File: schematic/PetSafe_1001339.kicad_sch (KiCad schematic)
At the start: 150 parts, among them J1 ICSP, J3 PIR BOARD, J5 MOTOR, J6 DNP, Q1 FMOS3401A?, Q11 MMBTA55?, Q2 BC847B?, Q3 MMBTA55?, Q4 MMBTA55?, Q5 MMBTA55?, Q6 MMBTA55?, Q7 BC857C?, Q8 SIL3724A?, Q9 DNP, U1 S-1200B45?, U106 U6A / DNP, U2 SN74LVC2G14DBV?, U3 SGM8542XS, U4 PIC16F18855, U5 MX512H, U6 S-812C33AMC? / 3.3V, U7 DNP, Y1 20 MHz

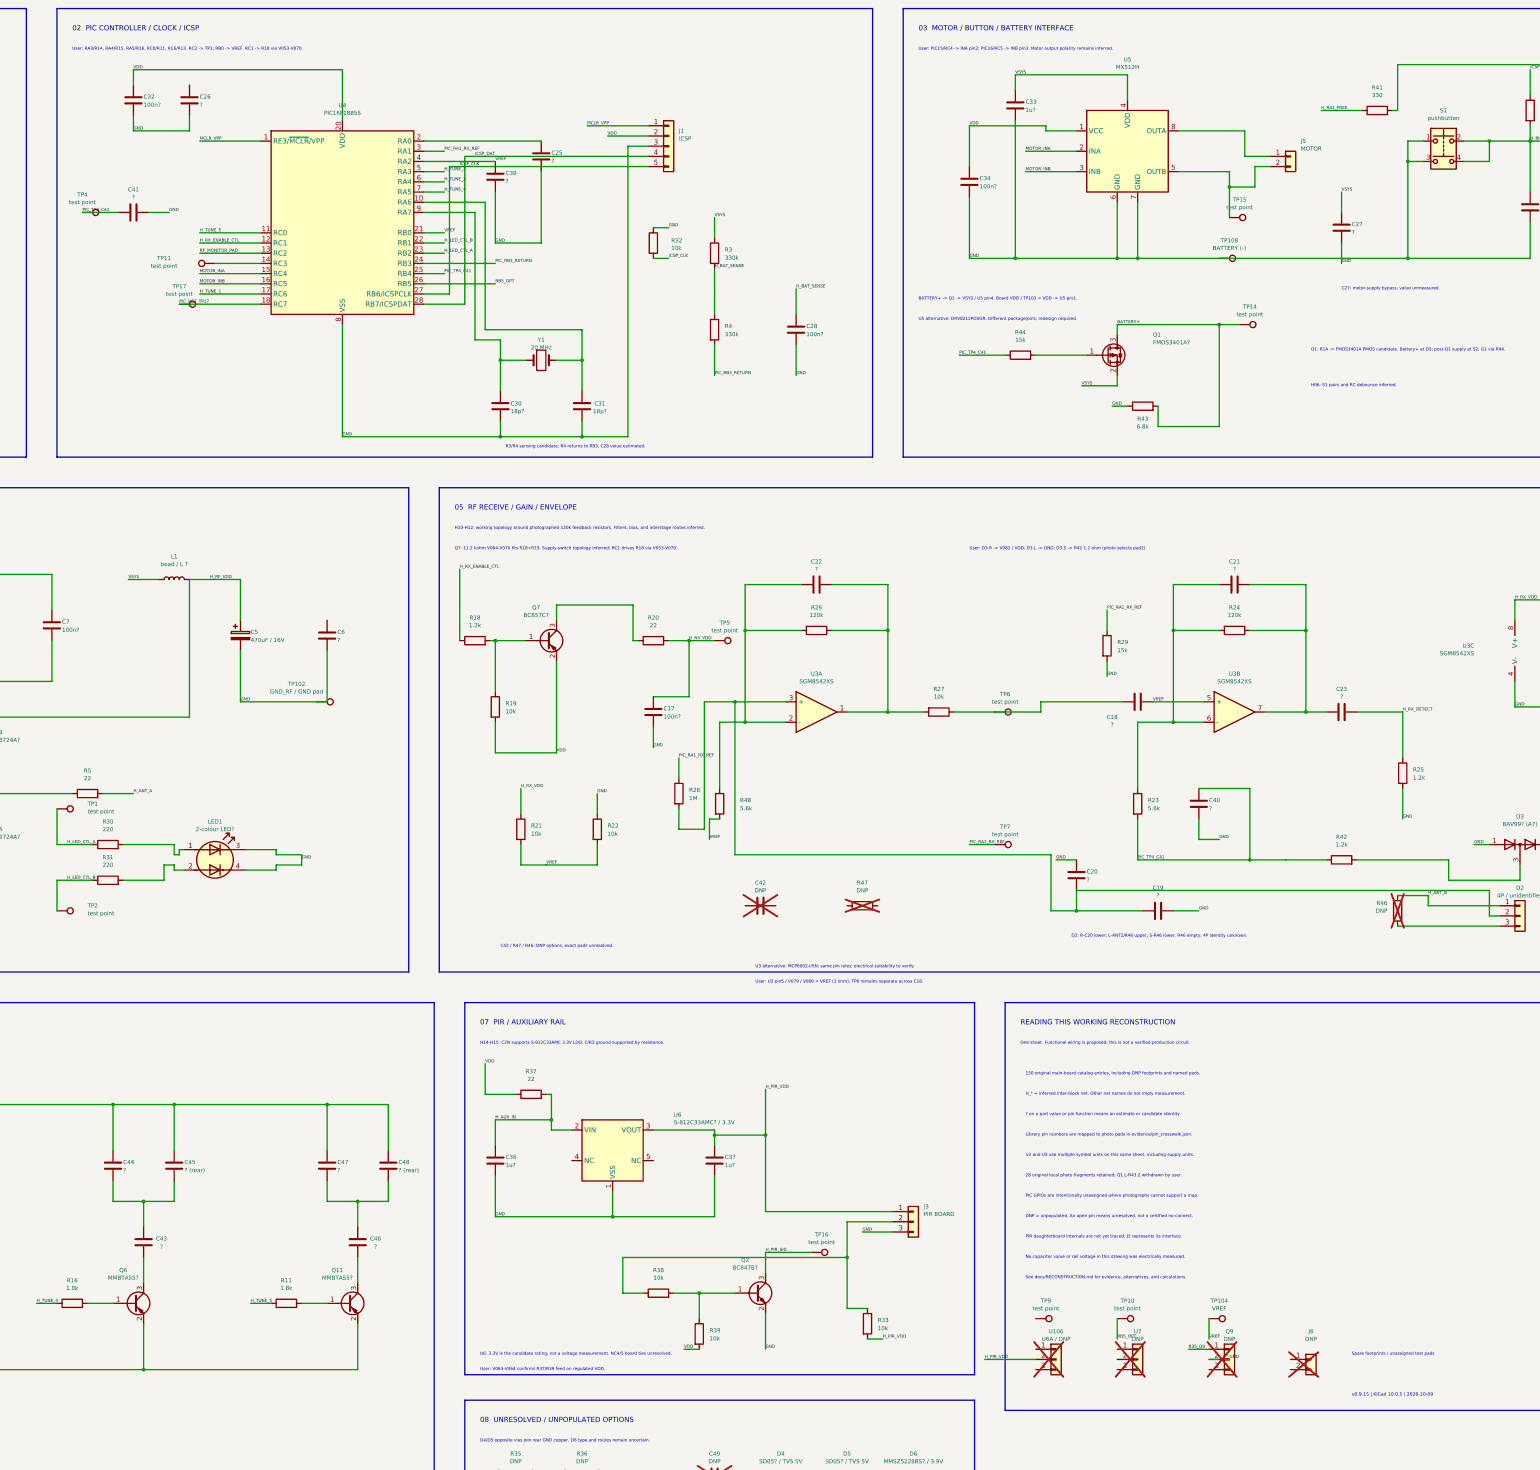
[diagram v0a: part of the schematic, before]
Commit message: Map U7 PIR connector and correct RB0 signal route
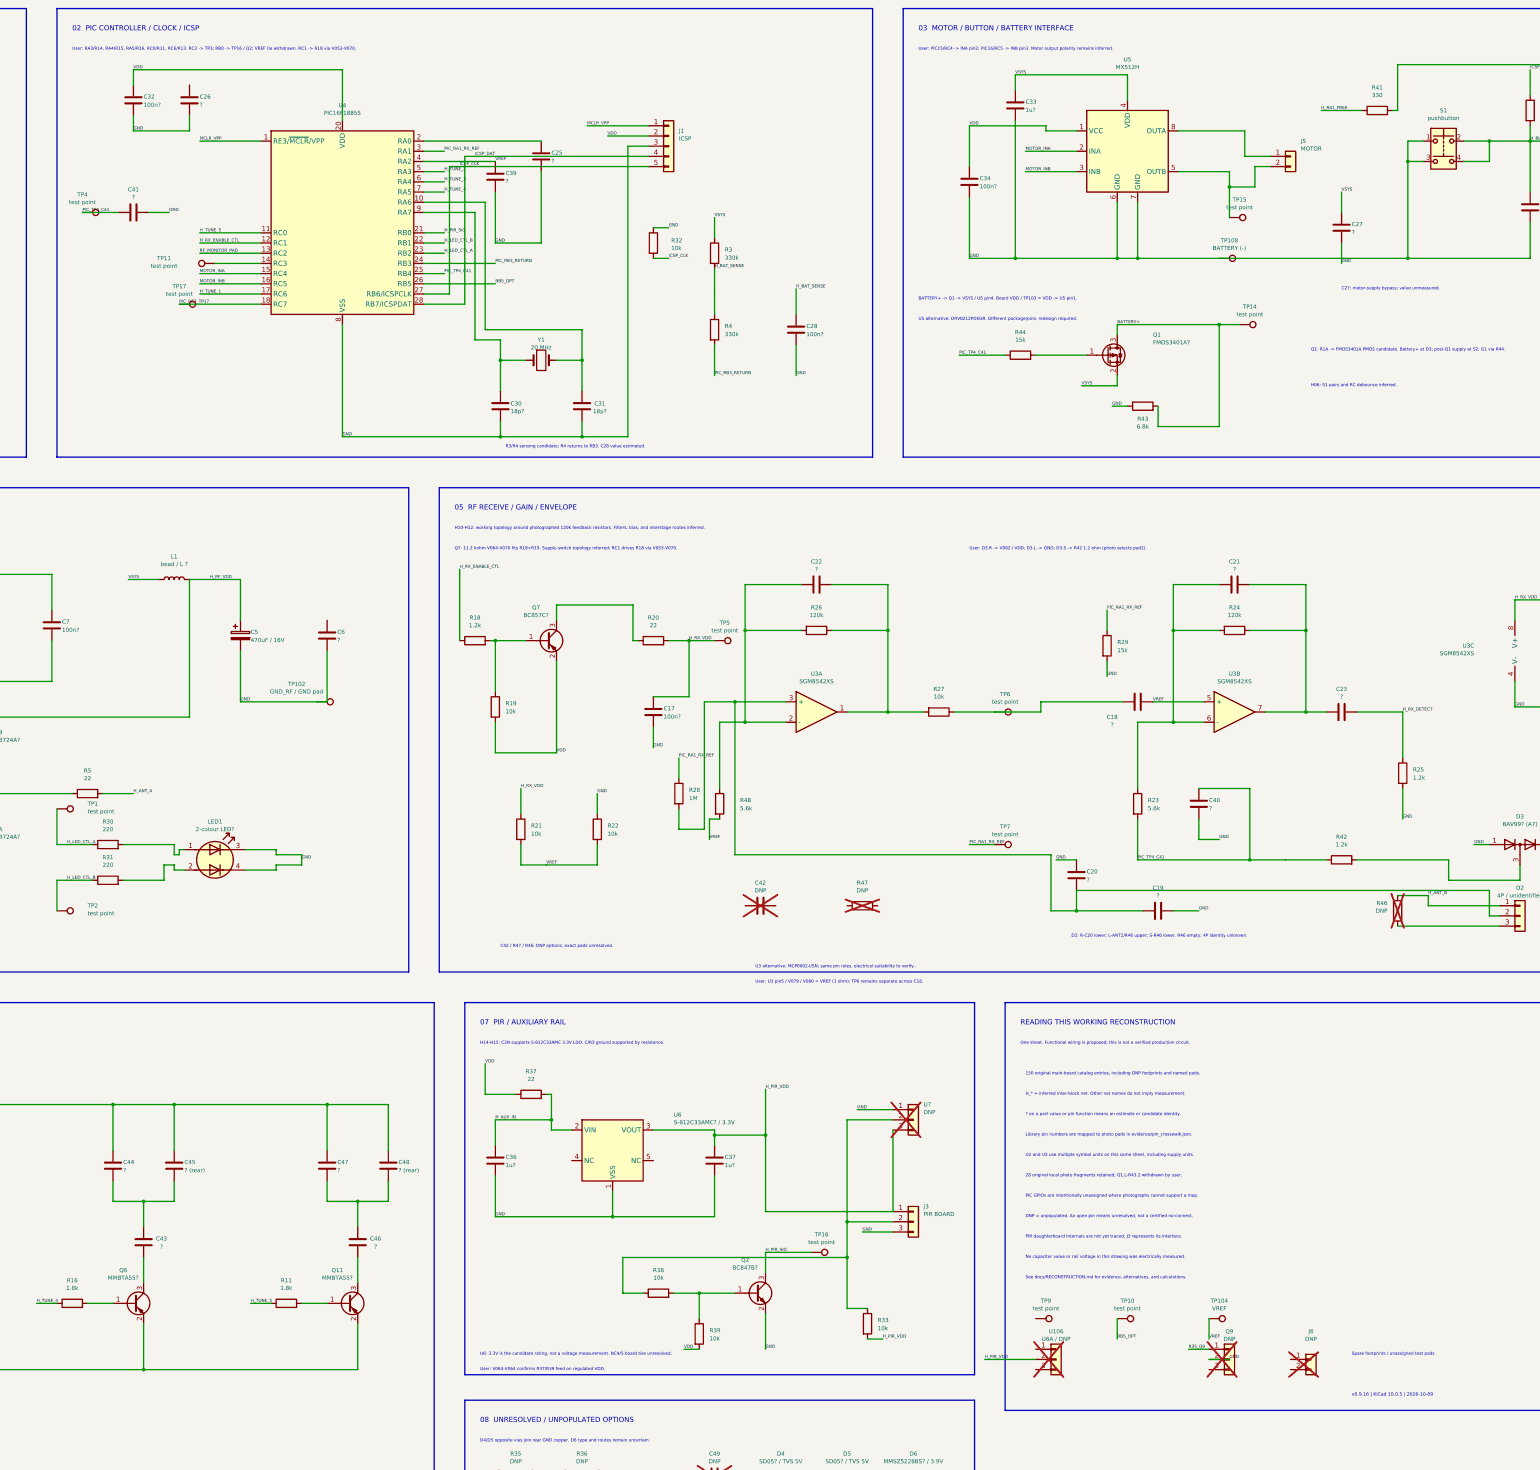
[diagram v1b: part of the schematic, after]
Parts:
- J3: MeasurementEvidence v0.9.14 user: pin1 PIR supply previously confirmed; pin2 H-R38 K/right/model1 1 ohm and H-R38 J/left/model2 10 kohm; pin3-GND 1 ohm. Pin2-GND remains 290 kohm (batch1), distinct from ground. Q2 onward/controller route remains unverified. -> v0.9.14 user: pin1 PIR supply previously confirmed; pin2 H-R38 K/right/model1 1 ohm and H-R38 J/left/model2 10 kohm; pin3-GND 1 ohm. Pin2-GND remains 290 kohm (batch1), distinct from ground. Q2 onward/controller route remains unverified. v0.9.16: matching physical columns reach U7; J3.1-U7.3 supply, J3.2-U7.2 signal, J3.3-U7.1 GND.; ViaEvidence v0.9.14 user: pin1 PIR supply previously confirmed; pin2 H-R38 K/right/model1 1 ohm and H-R38 J/left/model2 10 kohm; pin3-GND 1 ohm. Pin2-GND remains 290 kohm (batch1), distinct from ground. Q2 onward/controller route remains unverified. -> v0.9.14 user: pin1 PIR supply previously confirmed; pin2 H-R38 K/right/model1 1 ohm and H-R38 J/left/model2 10 kohm; pin3-GND 1 ohm. Pin2-GND remains 290 kohm (batch1), distinct from ground. Q2 onward/controller route remains unverified. v0.9.16: matching physical columns reach U7; J3.1-U7.3 supply, J3.2-U7.2 signal, J3.3-U7.1 GND.
- R21, R48: MeasurementEvidence (none) -> v0.9.16 CORRECTION: user confirms PIC21/RB0 -> TP16 -> Q2 s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; ViaEvidence v0.9.8: User confirms V071-VREF. Earlier V071-R21.2 and V02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 -> v0.9.16 CORRECTION: user confirms PIC21/RB0 -> TP16 -> Q2 s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
- R22: MeasurementEvidence v0.9.14 user: E/right/model1-GND 1 ohm; D/left/model2-VREF 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 -> v0.9.16 CORRECTION: user confirms PIC21/RB0 -> TP16 -> Q2 s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; ViaEvidence v0.9.14 user: E/right/model1-GND 1 ohm; D/left/model2-VREF 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 -> v0.9.16 CORRECTION: user confirms PIC21/RB0 -> TP16 -> Q2 s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
- TP104, U4: MeasurementEvidence (none) -> v0.9.16 CORRECTION: user confirms PIC21/RB0 -> TP16 -> Q2 s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; ViaEvidence v0.9.9: User checked V035-VREF TP. Prior photo association 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 -> v0.9.16 CORRECTION: user confirms PIC21/RB0 -> TP16 -> Q2 s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
- TP16: MeasurementEvidence (none) -> v0.9.16 CORRECTION: user confirms PIC21/RB0 -> TP16 -> Q2 s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; ViaEvidence (none) -> v0.9.16 CORRECTION: user confirms PIC21/RB0 -> TP16 -> Q2 s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
- U7: MeasurementEvidence (none) -> v0.9.16: user measured U7 square pad/model1 to J3.3/GND; mi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; ViaEvidence (none) -> v0.9.16: user measured U7 square pad/model1 to J3.3/GND; mi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
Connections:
- net GND: now also U7.1 (Pin_1)
- net H_PIR_SIG: now also U4.21 (RB0)
- net H_PIR_VDD: now also U7.3 (Pin_3)
- net VREF: no longer U4.21 (RB0)
- net at J3.2 (Pin_2), R33.1, R38.1: now also U7.2 (Pin_2)
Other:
- note added: "User: RA3/R14, RA4/R15, RA5/R16, RC0/R11, RC6/R13. RC2 -> TP3; RB0 -> TP16 / Q2; VREF tie withdrawn. RC1 -> R18 via V053-V070."
- note added: "v0.9.16 | KiCad 10.0.5 | 2026-10-09"
- note removed: "User: RA3/R14, RA4/R15, RA5/R16, RC0/R11, RC6/R13. RC2 -> TP3; RB0 -> VREF. RC1 -> R18 via V053-V070."
- note removed: "v0.9.15 | KiCad 10.0.5 | 2026-10-09"
- moved on the sheet: U7

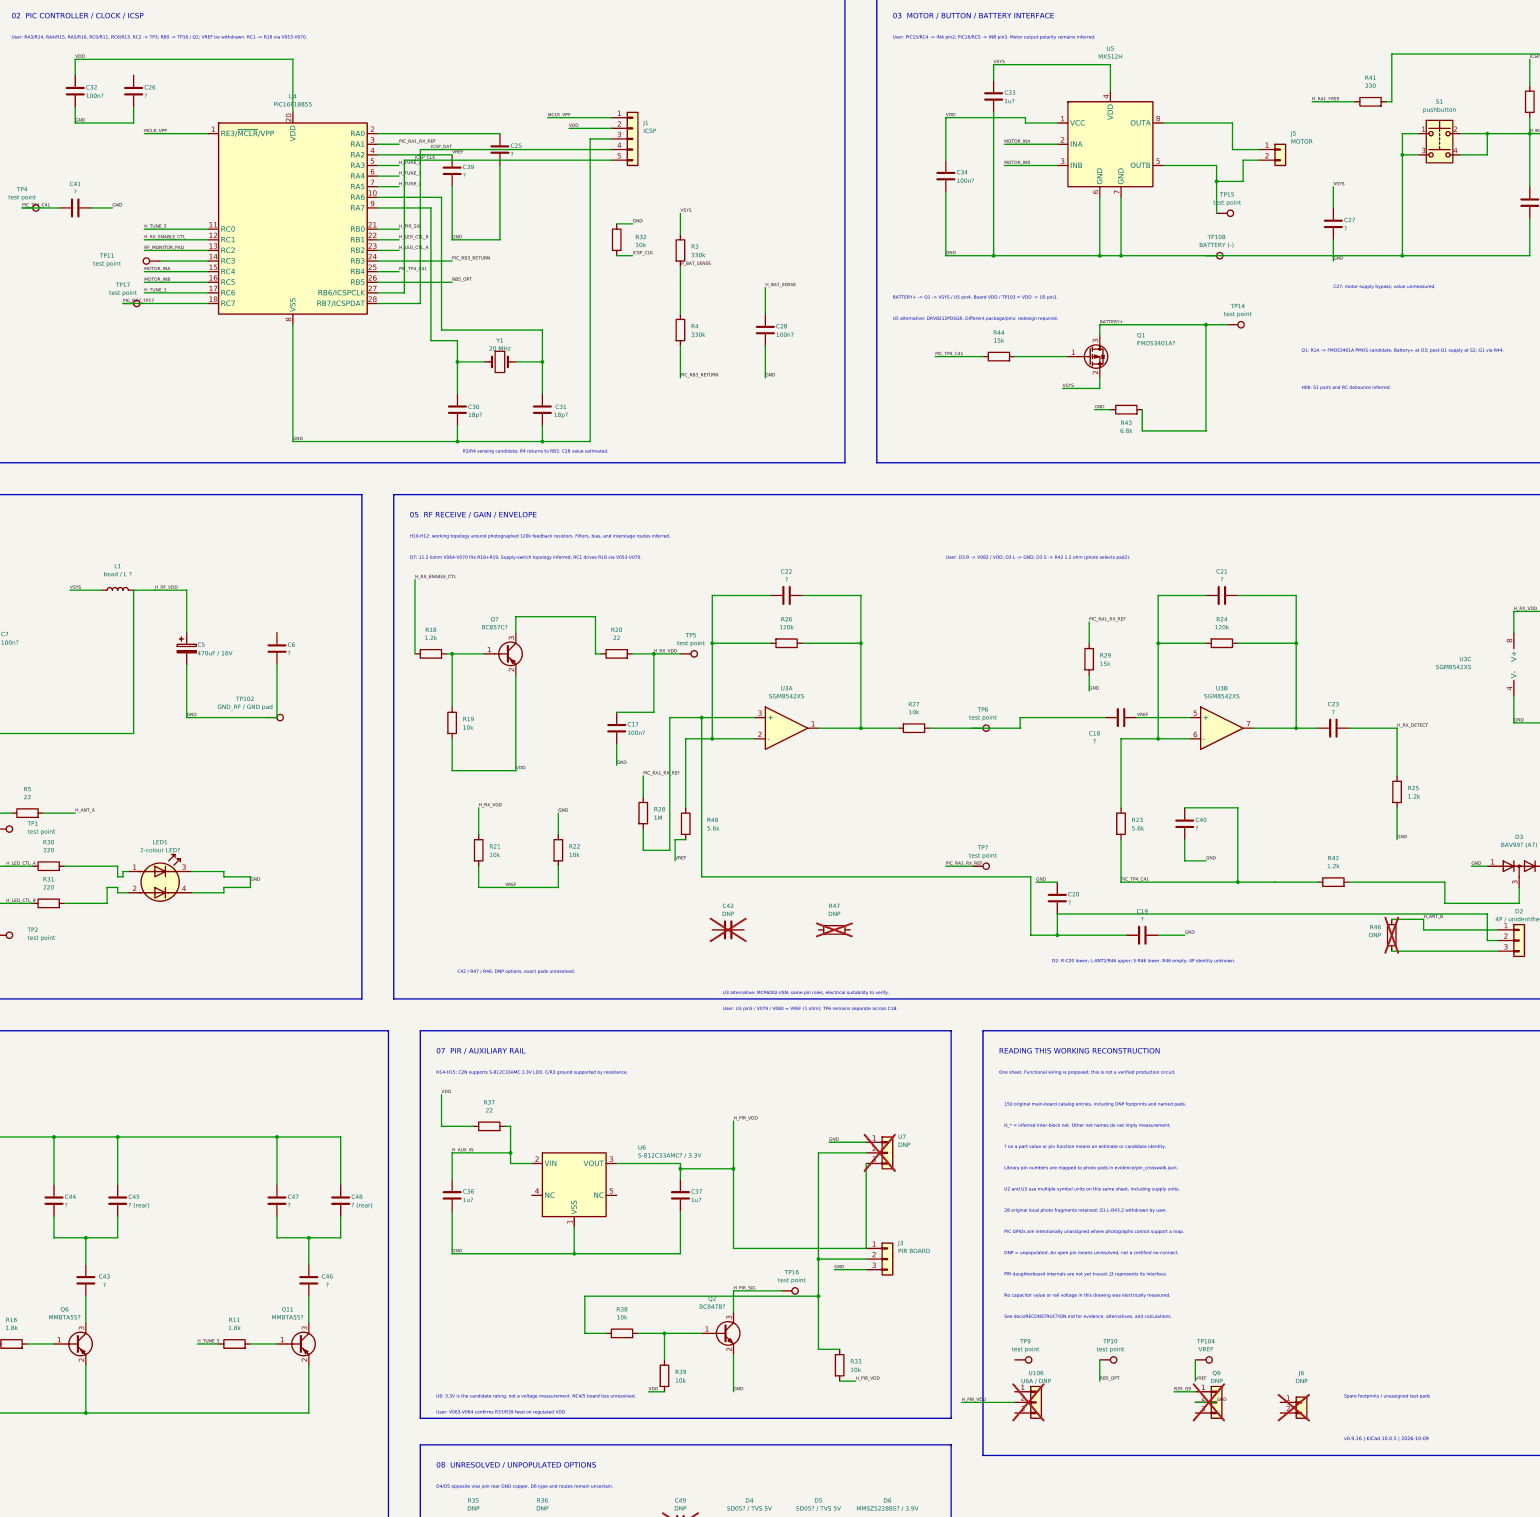
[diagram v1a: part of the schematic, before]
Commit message: Resolve C26 to PIC RA1 from annotated board photo
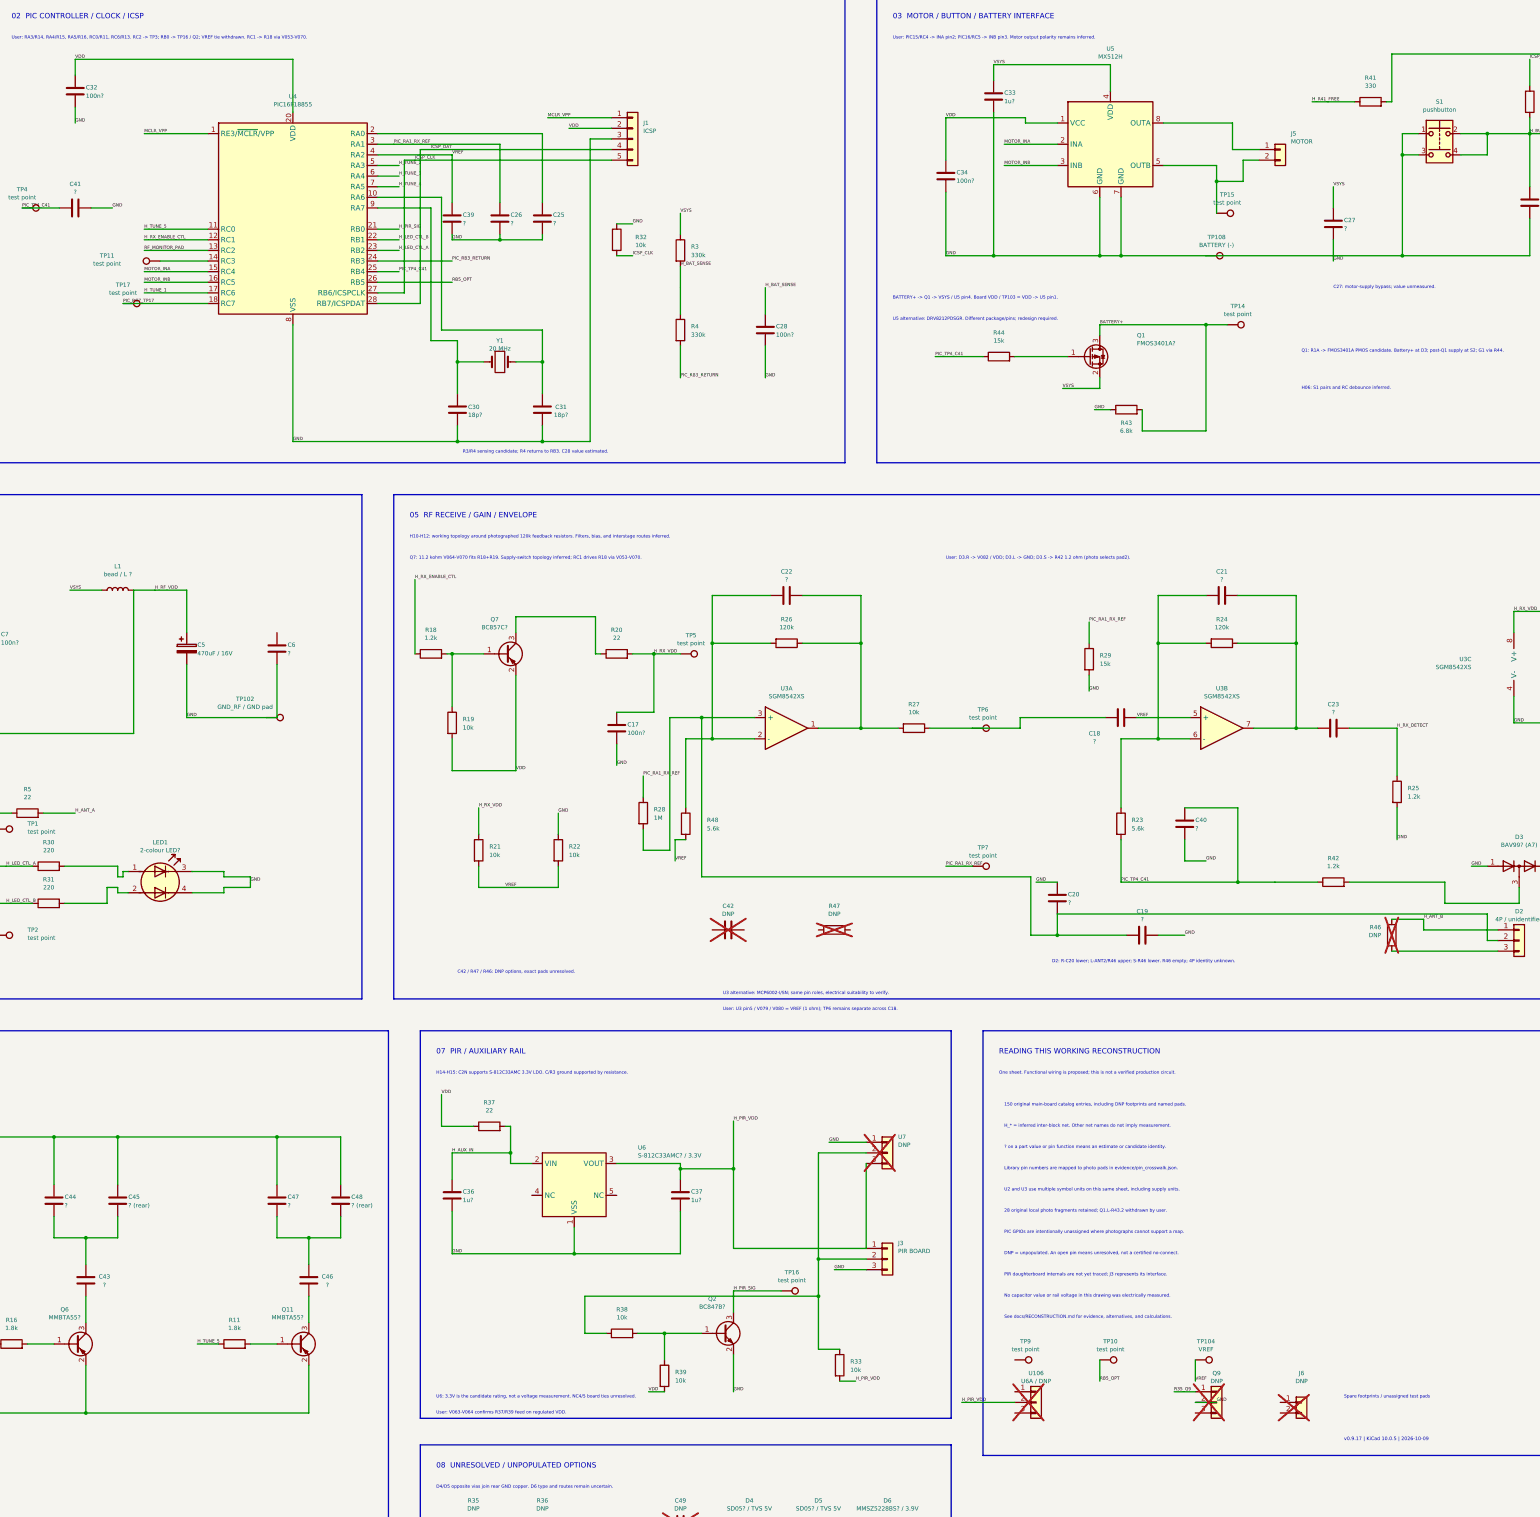
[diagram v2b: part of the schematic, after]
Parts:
- C25, C26, U4: ConnectionEvidence (none) -> v0.9.17 user-annotated photo: C25 right pad/model1 -> PIC2/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
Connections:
- net PIC_RA1_RX_REF: now also C26.1
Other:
- note added: "v0.9.17 | KiCad 10.0.5 | 2026-10-09"
- note removed: "v0.9.16 | KiCad 10.0.5 | 2026-10-09"
- moved on the sheet: C25, C26, C39
